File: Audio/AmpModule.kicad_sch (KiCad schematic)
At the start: 26 parts, among them J10 AMP_AUX_IN, J11 AMP_AUX_OUT, J9 AMP_PWR

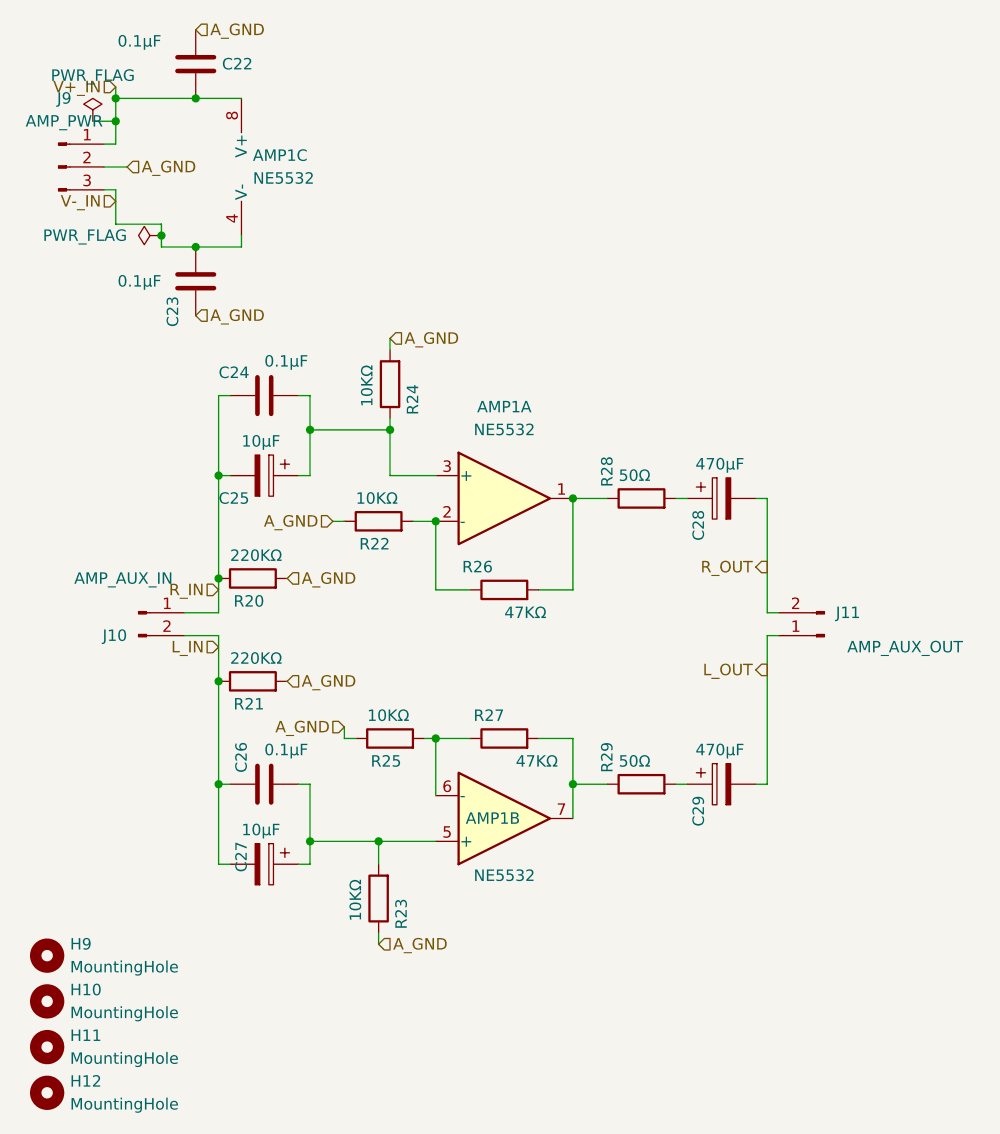
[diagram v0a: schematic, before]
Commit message: add controll module image
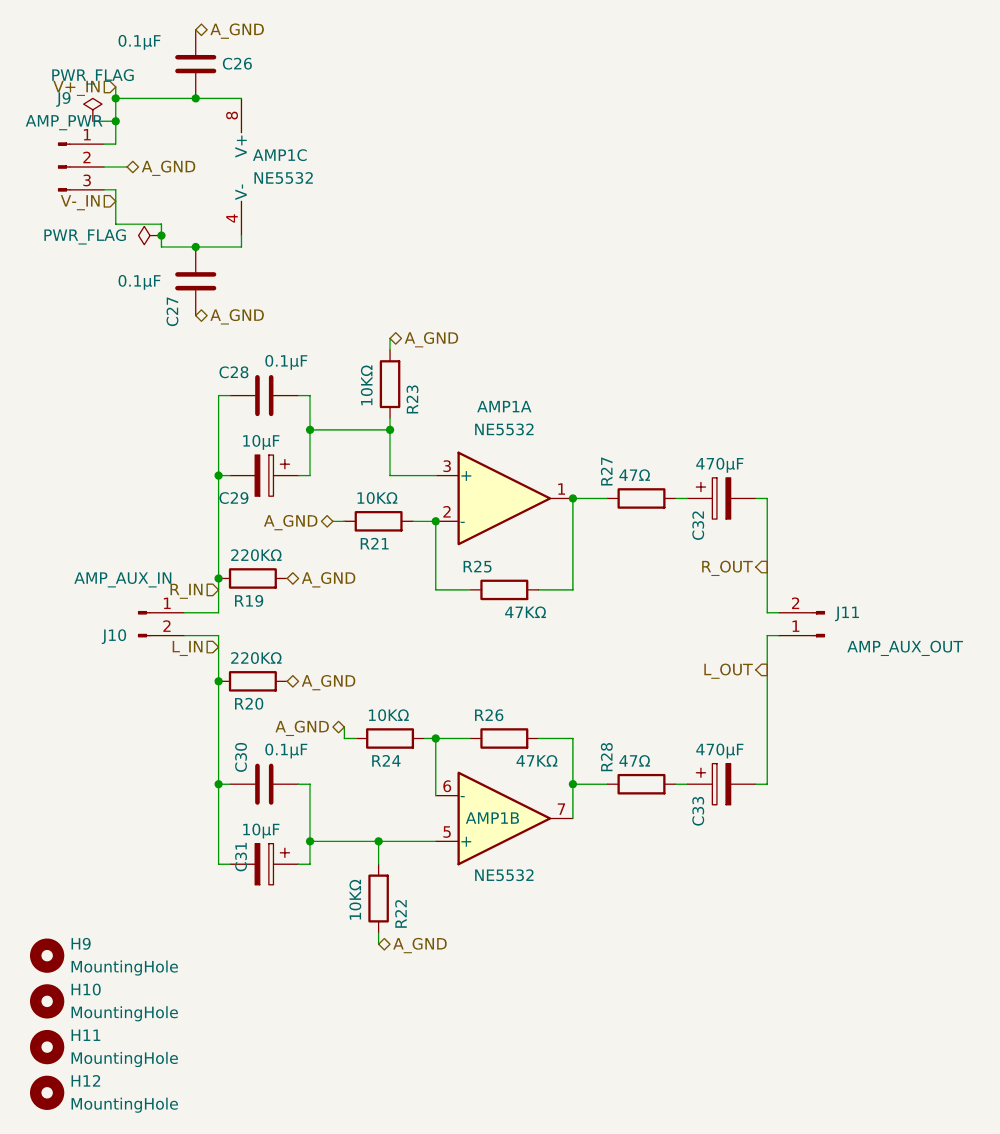
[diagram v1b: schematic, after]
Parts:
- R19: renamed from R20; footprint Resistor_SMD:R_0603_1608Metric_Pad0.98x0.95mm_HandSolder -> Resistor_SMD:R_1206_3216Metric_Pad1.30x1.75mm_HandSolder
- R20: renamed from R21; footprint Resistor_SMD:R_0603_1608Metric_Pad0.98x0.95mm_HandSolder -> Resistor_SMD:R_1206_3216Metric_Pad1.30x1.75mm_HandSolder
- R21: renamed from R22; footprint Resistor_SMD:R_0603_1608Metric_Pad0.98x0.95mm_HandSolder -> Resistor_SMD:R_1206_3216Metric_Pad1.30x1.75mm_HandSolder
- R22: renamed from R23; footprint Resistor_SMD:R_0603_1608Metric_Pad0.98x0.95mm_HandSolder -> Resistor_SMD:R_1206_3216Metric_Pad1.30x1.75mm_HandSolder
- R23: renamed from R24; footprint Resistor_SMD:R_0603_1608Metric_Pad0.98x0.95mm_HandSolder -> Resistor_SMD:R_1206_3216Metric_Pad1.30x1.75mm_HandSolder
- R24: renamed from R25; footprint Resistor_SMD:R_0603_1608Metric_Pad0.98x0.95mm_HandSolder -> Resistor_SMD:R_1206_3216Metric_Pad1.30x1.75mm_HandSolder
- R25: renamed from R26; footprint Resistor_SMD:R_0603_1608Metric_Pad0.98x0.95mm_HandSolder -> Resistor_SMD:R_1206_3216Metric_Pad1.30x1.75mm_HandSolder
- R26: renamed from R27; footprint Resistor_SMD:R_0603_1608Metric_Pad0.98x0.95mm_HandSolder -> Resistor_SMD:R_1206_3216Metric_Pad1.30x1.75mm_HandSolder
- R27: renamed from R28; value 50Ω -> 47Ω; footprint Resistor_SMD:R_0603_1608Metric_Pad0.98x0.95mm_HandSolder -> Resistor_SMD:R_1206_3216Metric_Pad1.30x1.75mm_HandSolder
- R28: renamed from R29; value 50Ω -> 47Ω; footprint Resistor_SMD:R_0603_1608Metric_Pad0.98x0.95mm_HandSolder -> Resistor_SMD:R_1206_3216Metric_Pad1.30x1.75mm_HandSolder
- renumbered C22 to C26, C23 to C27, C24 to C28, C25 to C29, C26 to C30, C27 to C31, C28 to C32, C29 to C33

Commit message: rework pcb
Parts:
- C26, C27: footprint Resistor_SMD:R_0603_1608Metric_Pad0.98x0.95mm_HandSolder -> Capacitor_SMD:C_1206_3216Metric_Pad1.33x1.80mm_HandSolder
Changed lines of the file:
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@@
-				)
-			)
-			(project "AmpModule"
-				(path "/9b212568-aead-45da-960b-770311cd62c9"
-					(reference "J10")
-					(unit 1)
 				)
 			)
@@
 				)
 			)
-			(project "AmpModule"
-				(path "/9b212568-aead-45da-960b-770311cd62c9"
-					(reference "C6")
-					(unit 1)
-				)
-			)
 		)
 	)
@@
 				)
 			)
-			(project "AmpModule"
-				(path "/9b212568-aead-45da-960b-770311cd62c9"
-					(reference "R4")
-					(unit 1)
-				)
-			)
 		)
 	)
@@
 				)
 			)
-			(project "AmpModule"
-				(path "/9b212568-aead-45da-960b-770311cd62c9"
-					(reference "J11")
-					(unit 1)
-				)
-			)
 		)
 	)
@@
 				(path "/760b9589-09e7-434e-9ca2-6e4136e3b7a2/477be123-54b6-4d91-ae02-fb2ccb128622"
 					(reference "R23")
-					(unit 1)
-				)
-			)
-			(project "AmpModule"
-				(path "/9b212568-aead-45da-960b-770311cd62c9"
-					(reference "R24")
 					(unit 1)
 				)
@@
 				)
 			)
-			(project "AmpModule"
-				(path "/9b212568-aead-45da-960b-770311cd62c9"
-					(reference "U1")
-					(unit 1)
-				)
-			)
 		)
 	)
@@
 				(path "/760b9589-09e7-434e-9ca2-6e4136e3b7a2/477be123-54b6-4d91-ae02-fb2ccb128622"
 					(reference "R20")
-					(unit 1)
-				)
-			)
-			(project "AmpModule"
-				(path "/9b212568-aead-45da-960b-770311cd62c9"
-					(reference "R21")
 					(unit 1)
 				)
@@
 				)
 			)
-			(project "AmpModule"
-				(path "/9b212568-aead-45da-960b-770311cd62c9"
-					(reference "U1")
-					(unit 2)
-				)
-			)
 		)
 	)
@@
 				)
 			)
-			(project "AmpModule"
-				(path "/9b212568-aead-45da-960b-770311cd62c9"
-					(reference "H10")
-					(unit 1)
-				)
-			)
 		)
 	)
@@
 				)
 			)
-			(project "AmpModule"
-				(path "/9b212568-aead-45da-960b-770311cd62c9"
-					(reference "J9")
-					(unit 1)
-				)
-			)
 		)
 	)
@@
 				)
 			)
-			(project "AmpModule"
-				(path "/9b212568-aead-45da-960b-770311cd62c9"
-					(reference "C3")
-					(unit 1)
-				)
-			)
 		)
 	)
@@
 				(path "/760b9589-09e7-434e-9ca2-6e4136e3b7a2/477be123-54b6-4d91-ae02-fb2ccb128622"
 					(reference "R22")
-					(unit 1)
-				)
-			)
-			(project "AmpModule"
-				(path "/9b212568-aead-45da-960b-770311cd62c9"
-					(reference "R23")
 					(unit 1)
 				)
@@
 				)
 			)
-			(project "AmpModule"
-				(path "/9b212568-aead-45da-960b-770311cd62c9"
-					(reference "C8")
-					(unit 1)
-				)
-			)
 		)
 	)
@@
 				)
 			)
-			(project "AmpModule"
-				(path "/9b212568-aead-45da-960b-770311cd62c9"
-					(reference "H12")
-					(unit 1)
-				)
-			)
 		)
 	)
@@
 				)
 			)
-			(project "AmpModule"
-				(path "/9b212568-aead-45da-960b-770311cd62c9"
-					(reference "C5")
-					(unit 1)
-				)
-			)
 		)
 	)
@@
 				(path "/760b9589-09e7-434e-9ca2-6e4136e3b7a2/477be123-54b6-4d91-ae02-fb2ccb128622"
 					(reference "R27")
-					(unit 1)
-				)
-			)
-			(project "AmpModule"
-				(path "/9b212568-aead-45da-960b-770311cd62c9"
-					(reference "R9")
 					(unit 1)
 				)
@@
 			)
 		)
-		(property "Footprint" "Resistor_SMD:R_0603_1608Metric_Pad0.98x0.95mm_HandSolder"
+		(property "Footprint" "Capacitor_SMD:C_1206_3216Metric_Pad1.33x1.80mm_HandSolder"
 			(at 32.0548 52.07 0)
 			(hide yes)
@@
 				(path "/760b9589-09e7-434e-9ca2-6e4136e3b7a2/477be123-54b6-4d91-ae02-fb2ccb128622"
 					(reference "C27")
-					(unit 1)
-				)
-			)
-			(project "AmpModule"
-				(path "/9b212568-aead-45da-960b-770311cd62c9"
-					(reference "C23")
 					(unit 1)
 				)
@@
 				)
 			)
-			(project "AmpModule"
-				(path "/9b212568-aead-45da-960b-770311cd62c9"
-					(reference "C7")
-					(unit 1)
-				)
-			)
 		)
 	)
@@
 				)
 			)
-			(project "AmpModule"
-				(path "/9b212568-aead-45da-960b-770311cd62c9"
-					(reference "#FLG07")
-					(unit 1)
-				)
-			)
 		)
 	)
@@
 				)
 			)
-			(project "AmpModule"
-				(path "/9b212568-aead-45da-960b-770311cd62c9"
-					(reference "U1")
-					(unit 3)
-				)
-			)
 		)
 	)
@@
 				)
 			)
-			(project "AmpModule"
-				(path "/9b212568-aead-45da-960b-770311cd62c9"
-					(reference "R7")
-					(unit 1)
-				)
-			)
 		)
 	)
@@
 				(path "/760b9589-09e7-434e-9ca2-6e4136e3b7a2/477be123-54b6-4d91-ae02-fb2ccb128622"
 					(reference "R24")
-					(unit 1)
-				)
-			)
-			(project "AmpModule"
-				(path "/9b212568-aead-45da-960b-770311cd62c9"
-					(reference "R25")
 					(unit 1)
 				)
@@
 			)
 		)
-		(property "Footprint" "Resistor_SMD:R_0603_1608Metric_Pad0.98x0.95mm_HandSolder"
+		(property "Footprint" "Capacitor_SMD:C_1206_3216Metric_Pad1.33x1.80mm_HandSolder"
 			(at 32.0548 27.94 0)
 			(hide yes)
@@
 				)
 			)
-			(project "AmpModule"
-				(path "/9b212568-aead-45da-960b-770311cd62c9"
-					(reference "C22")
-					(unit 1)
-				)
-			)
 		)
 	)
@@
 				(path "/760b9589-09e7-434e-9ca2-6e4136e3b7a2/477be123-54b6-4d91-ae02-fb2ccb128622"
 					(reference "C29")
-					(unit 1)
-				)
-			)
-			(project "AmpModule"
-				(path "/9b212568-aead-45da-960b-770311cd62c9"
-					(reference "C4")
 					(unit 1)
 				)
@@
 				)
 			)
-			(project "AmpModule"
-				(path "/9b212568-aead-45da-960b-770311cd62c9"
-					(reference "H9")
-					(unit 1)
-				)
-			)
 		)
 	)
@@
 				(path "/760b9589-09e7-434e-9ca2-6e4136e3b7a2/477be123-54b6-4d91-ae02-fb2ccb128622"
 					(reference "R28")
-					(unit 1)
-				)
-			)
-			(project "AmpModule"
-				(path "/9b212568-aead-45da-960b-770311cd62c9"
-					(reference "R10")
 					(unit 1)
 				)
@@
 				)
 			)
-			(project "AmpModule"
-				(path "/9b212568-aead-45da-960b-770311cd62c9"
-					(reference "H11")
-					(unit 1)
-				)
-			)
 		)
 	)
@@
 				(path "/760b9589-09e7-434e-9ca2-6e4136e3b7a2/477be123-54b6-4d91-ae02-fb2ccb128622"
 					(reference "R26")
-					(unit 1)
-				)
-			)
-			(project "AmpModule"
-				(path "/9b212568-aead-45da-960b-770311cd62c9"
-					(reference "R8")
 					(unit 1)
 				)
@@
 				)
 			)
-			(project "AmpModule"
-				(path "/9b212568-aead-45da-960b-770311cd62c9"
-					(reference "#FLG06")
-					(unit 1)
-				)
-			)
 		)
 	)
@@
 					(unit 1)
 				)
-			)
-			(project "AmpModule"
-				(path "/9b212568-aead-45da-960b-770311cd62c9"
-					(reference "R20")
-					(unit 1)
-				)

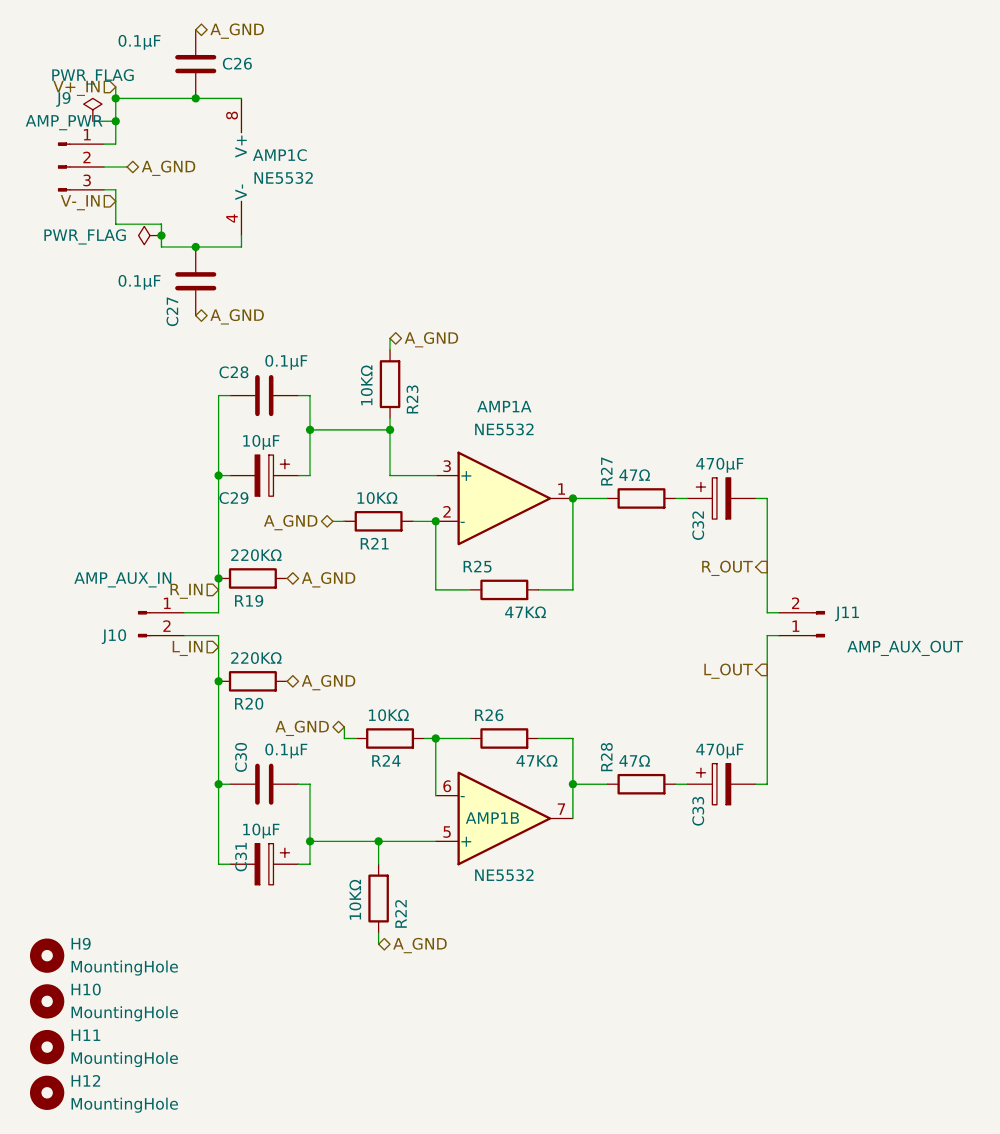
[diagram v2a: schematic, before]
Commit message: add relay
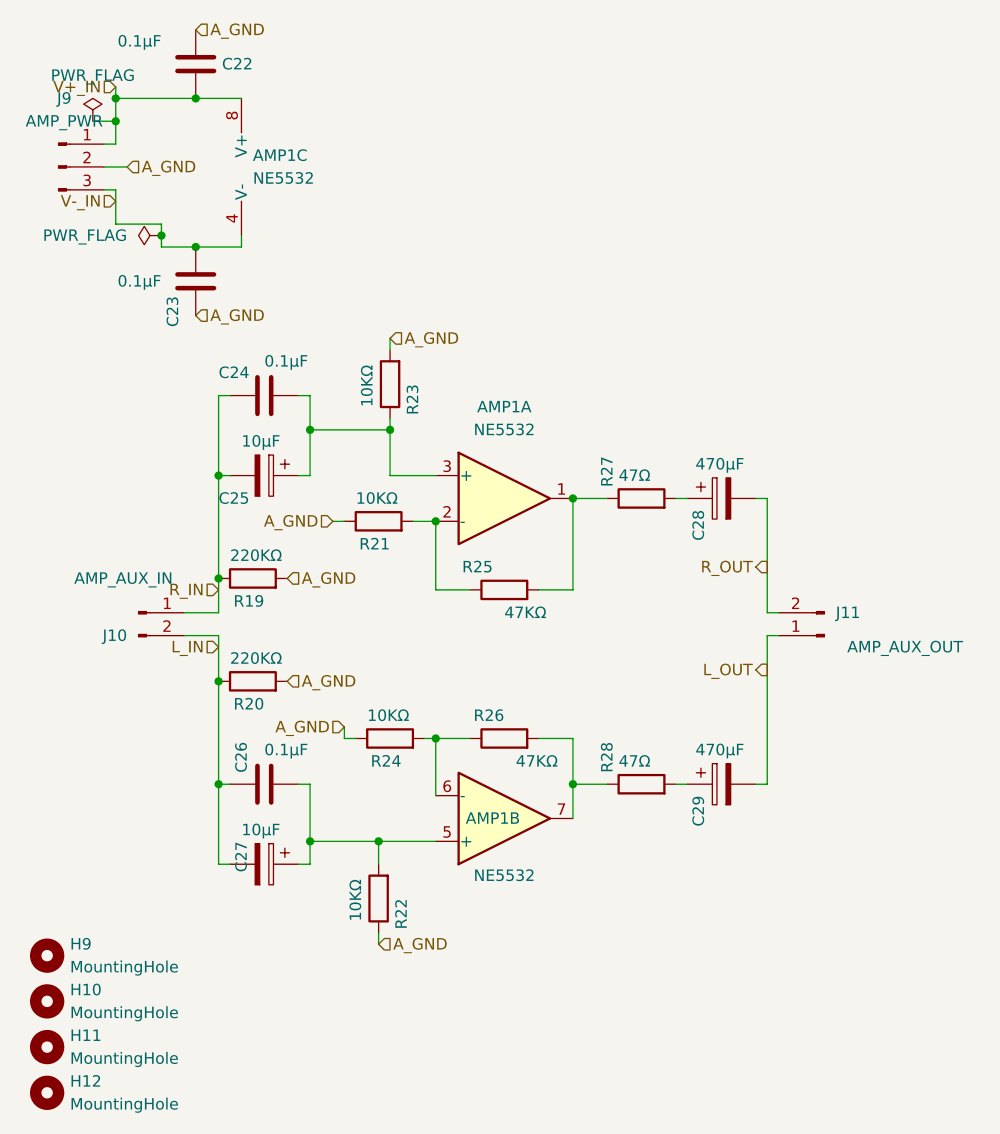
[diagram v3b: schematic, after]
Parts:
- C22: renamed from C26; footprint Capacitor_SMD:C_1206_3216Metric_Pad1.33x1.80mm_HandSolder -> Resistor_SMD:R_0603_1608Metric_Pad0.98x0.95mm_HandSolder
- C23: renamed from C27; footprint Capacitor_SMD:C_1206_3216Metric_Pad1.33x1.80mm_HandSolder -> Resistor_SMD:R_0603_1608Metric_Pad0.98x0.95mm_HandSolder
- R19, R20, R21, R22, R23, R24, R25, R26, R27, R28: footprint Resistor_SMD:R_1206_3216Metric_Pad1.30x1.75mm_HandSolder -> Resistor_SMD:R_0603_1608Metric_Pad0.98x0.95mm_HandSolder
- renumbered C28 to C24, C29 to C25, C30 to C26, C31 to C27, C32 to C28, C33 to C29
